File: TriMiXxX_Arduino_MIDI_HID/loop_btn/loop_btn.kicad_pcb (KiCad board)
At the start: 2 copper layers, 109 x 38.1 mm, 22 parts, among them J6 LOOP, SW1 SW_START, SW2 SW_END, SW3 SW_RELOOP

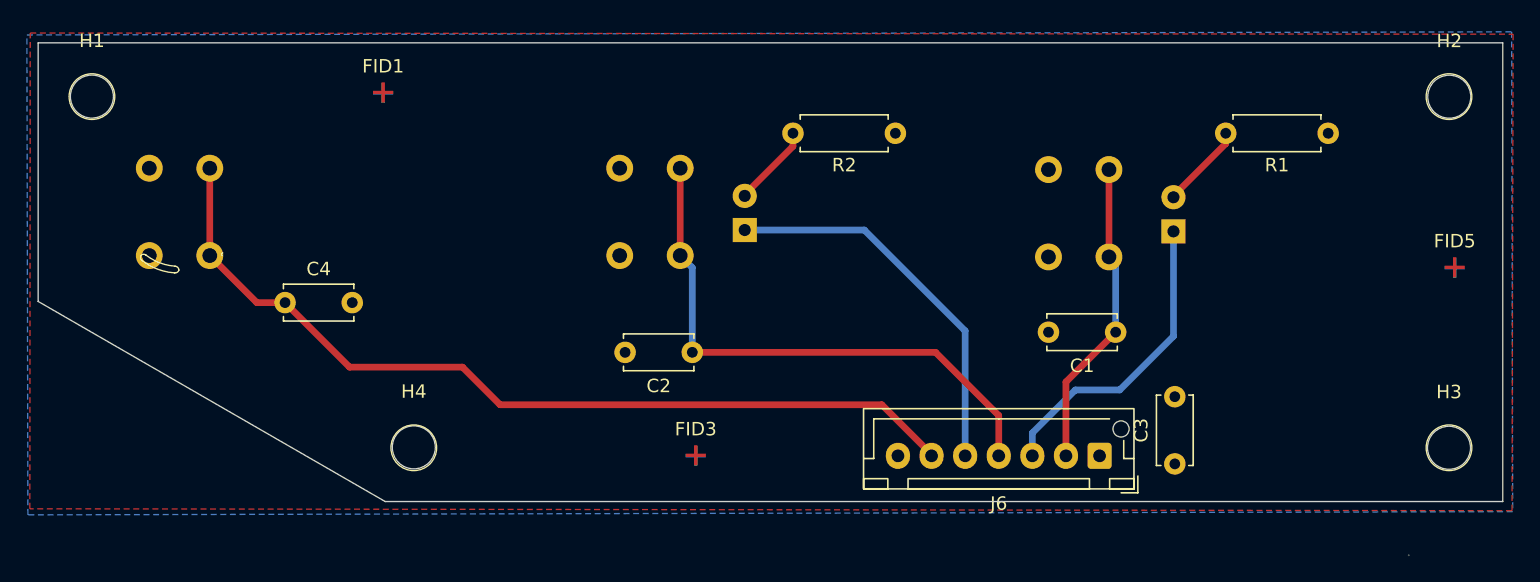
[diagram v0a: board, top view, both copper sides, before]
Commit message: Update schematics for jlcpcb productions, new dims, and sunlu petgcf calibration
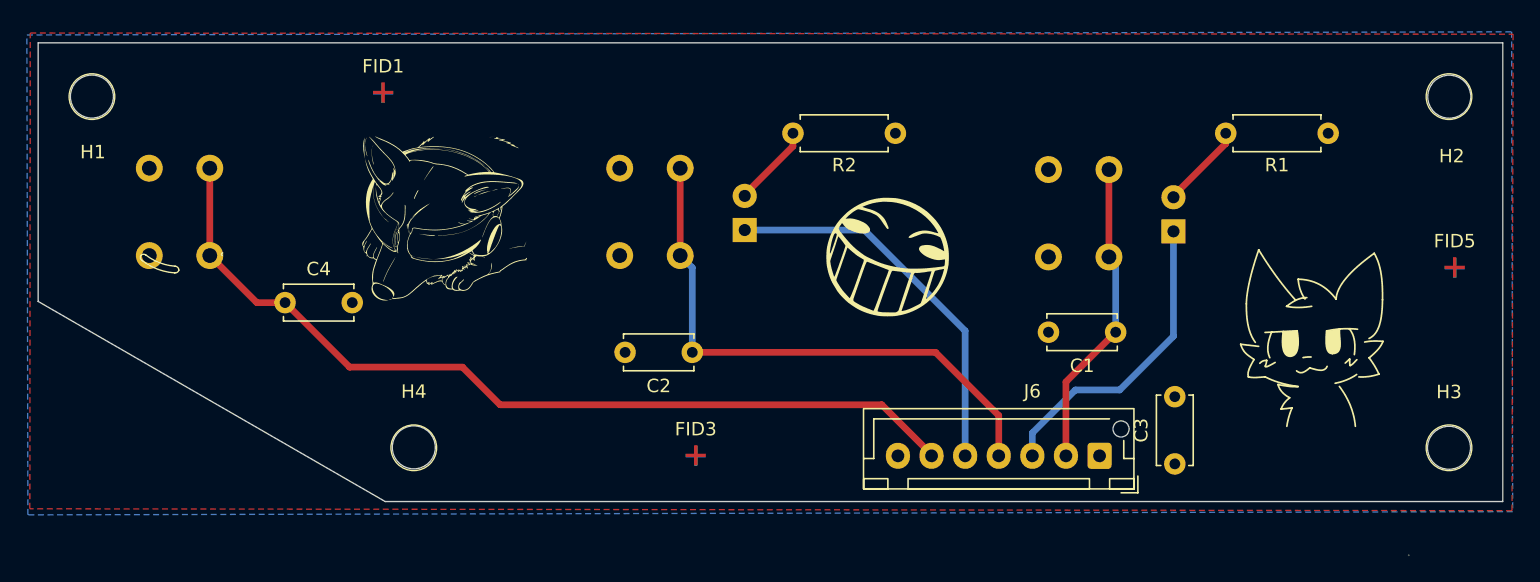
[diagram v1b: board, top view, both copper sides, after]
